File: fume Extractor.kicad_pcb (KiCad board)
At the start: 2 copper layers, 63.5 x 23.5 mm, 11 parts, among them J1 FAN, Q1 BC337, SW1 SW_SPST, U1 L7805ACV

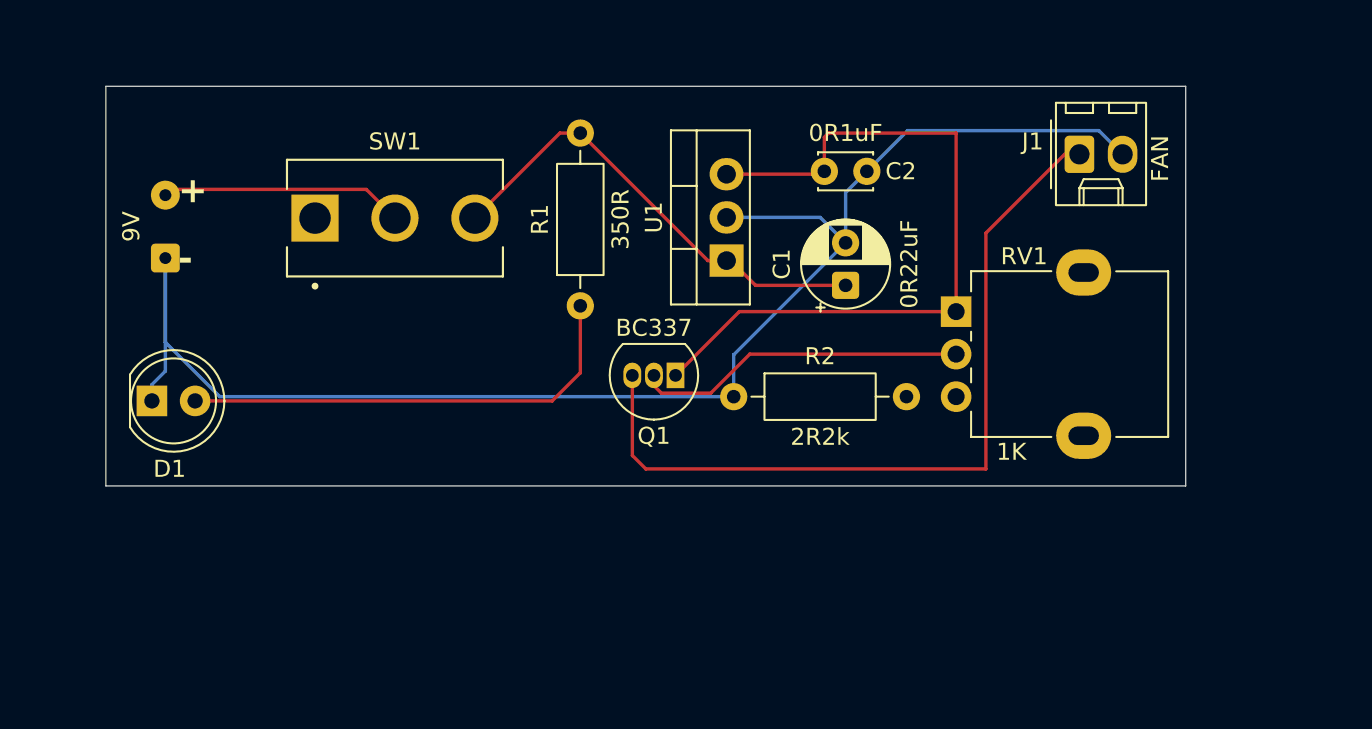
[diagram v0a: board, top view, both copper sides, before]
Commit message: fix: adjust pp cap and sizes
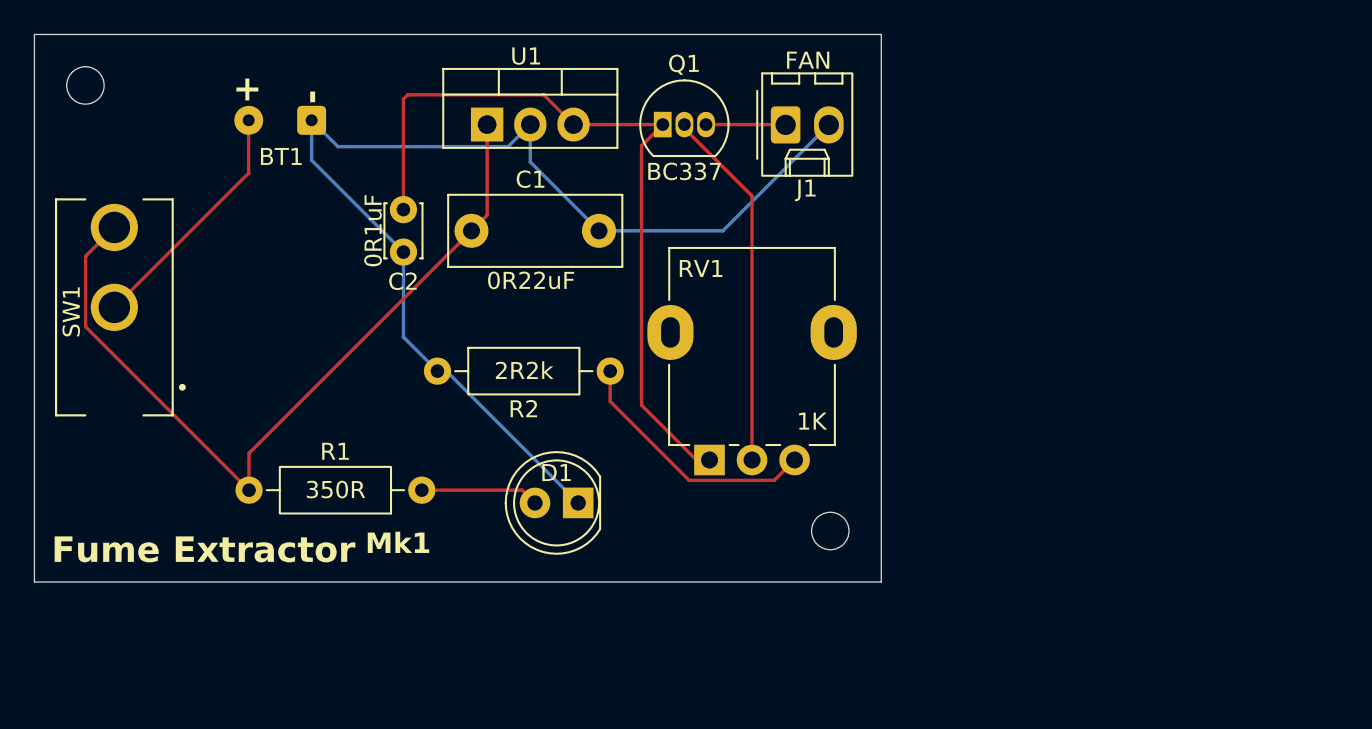
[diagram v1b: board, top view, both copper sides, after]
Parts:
- added ?: MountingHole_2.2mm_M2, MountingHole:MountingHole_2.2mm_M2, F.Cu at (69.8, 57.2)
- added REF**: MountingHole_2.2mm_M2, MountingHole:MountingHole_2.2mm_M2, F.Cu at (113.6, 83.4)
- C1: footprint Capacitor_THT:CP_Radial_D5.0mm_P2.50mm -> Capacitor_THT:C_Rect_L10.0mm_W4.0mm_P7.50mm_MKS4
- moved C2 27.7 mm to (88.5, 67.0), turned to 90 degrees
- moved D1 25.8 mm to (98.8, 81.8), turned to 180 degrees
- moved C1 22.2 mm to (92.5, 65.8), turned to 0 degrees
- moved R2 17.5 mm to (90.5, 74.0)
- moved J1 17.4 mm to (111.0, 59.5)
- moved SW1 17.3 mm to (71.5, 70.2), turned to 180 degrees
- moved RV1 16.9 mm to (106.5, 79.2), turned to 90 degrees
- moved U1 16.2 mm to (93.4, 59.5), turned to 0 degrees
- moved Q1 14.8 mm to (103.8, 59.5), turned to 0 degrees
- moved R1 14.3 mm to (89.6, 81.0), turned to 180 degrees
- moved BT1 6.59 mm to (79.4, 59.2), turned to 0 degrees
- renumbered 9V to BT1
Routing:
- net Net-(J1-VCC): track 47.1 -> 4.69 mm
- net -BATT: track 90.3 -> 67.4 mm
- net Net-(D1-Pad2): track 27.3 -> 6.97 mm
- net Net-(U1-IN): track 27.6 -> 47.4 mm
- net Net-(R2-Pad2): track 0.00 -> 15.0 mm
- net Net-(Q1-B): track 19.5 -> 21.4 mm
- net Net-(Q1-C): track 44.2 -> 44.9 mm
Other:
- board size 63.5 x 23.5 mm -> 49.8 x 32.2 mm
- board text added: "Fume Extractor^{ Mk1}"
- board text added: "WayWayWay"
- board text added: "^{Design:} Lucas Santos"

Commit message: feat: v2 with trimmer pot
Added RV2 to avoid long dead zones in RV1 because 500ohm is too much to
limit the 2V needed to minimally drive the fan, so the pot is largelly
dead. Adding a 1k 3266 Trimmer increases the ground resistance and the
floor voltage so we need to turn RV1 less to start the fan.

Plus, this gives a finer control over the fan speed itself
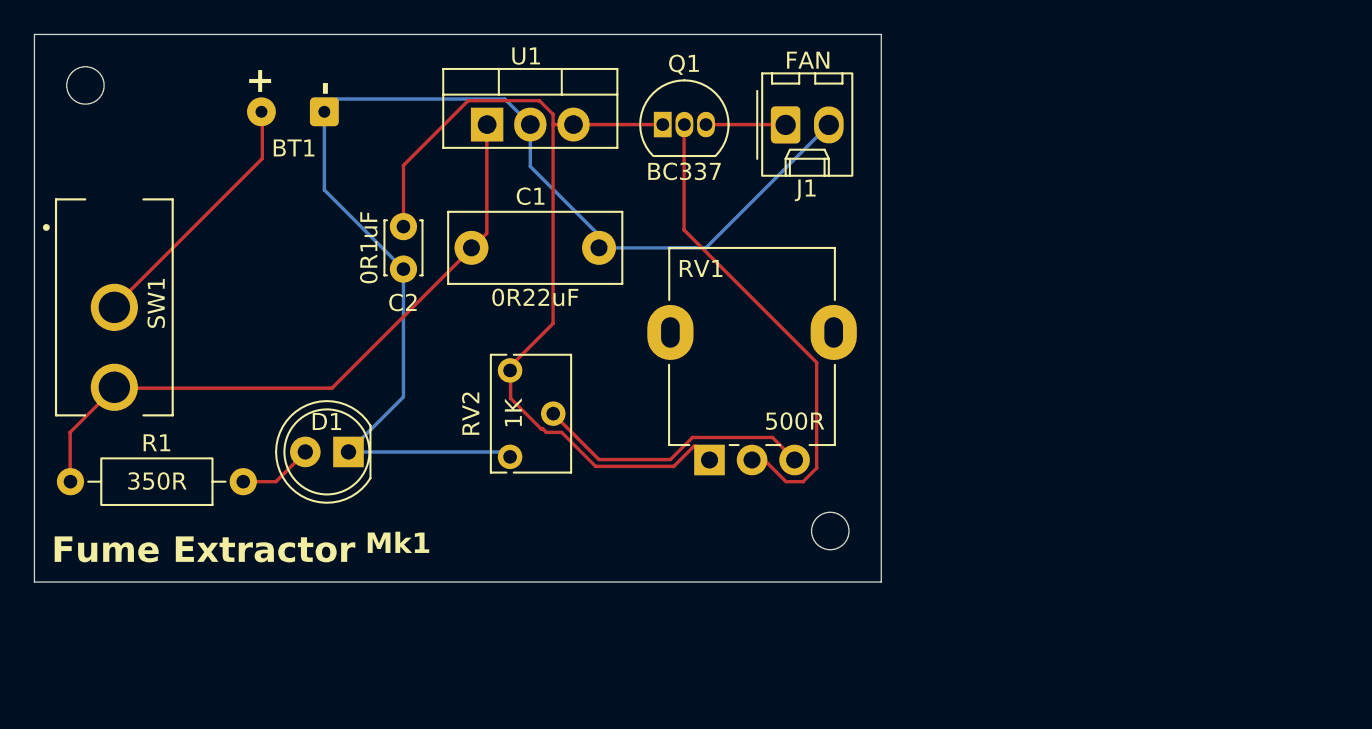
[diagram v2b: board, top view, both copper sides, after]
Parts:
- removed R2: 2R2k, Resistor_THT:R_Axial_DIN0207_L6.3mm_D2.5mm_P10.16mm_Horizontal
- added RV2: 1K, Potentiometer_THT:Potentiometer_Bourns_3266W_Vertical, F.Cu at (94.8, 74.0)
- RV1: value 1K -> 500R
- moved D1 13.8 mm to (85.3, 78.8)
- moved R1 10.5 mm to (79.1, 80.5)
- moved C1 1.00 mm to (92.5, 66.8)
- moved C2 1.00 mm to (88.5, 68.0)
- moved BT1 0.90 mm to (80.2, 58.8)
- turned SW1 to 0 degrees
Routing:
- net Net-(U1-IN): track 47.4 -> 38.6 mm
- net Net-(Q1-C): track 44.9 -> 52.4 mm
- net Net-(Q1-B): track 21.4 -> 28.1 mm
- net -BATT: track 67.4 -> 71.4 mm
- net Net-(D1-Pad2): track 6.97 -> 4.30 mm
- net Net-(RV1-Pad3): track 15.0 -> 16.4 mm
- net +9V: track 14.3 -> 15.0 mm

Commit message: Add Version 2
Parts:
- removed ?: MountingHole_2.2mm_M2, MountingHole:MountingHole_2.2mm_M2
- removed the REF** at (113.6, 83.4)
- added REF**: MountingHole_2.2mm_M2, MountingHole:MountingHole_2.2mm_M2, F.Cu at (104.4, 80.7)
- added REF**: MountingHole_2.2mm_M2, MountingHole:MountingHole_2.2mm_M2, F.Cu at (140.8, 90.3)
- BT1: footprint Connector_Wire:SolderWire-0.127sqmm_1x02_P3.7mm_D0.48mm_OD1mm -> Connector_Molex:Molex_KK-254_AE-6410-02A_1x02_P2.54mm_Vertical
- D1: value LED_5mm -> LED_3mm; footprint LED_THT:LED_D5.0mm -> LED_THT:LED_D3.0mm
- RV1: footprint Potentiometer_THT:Potentiometer_Alpha_RD901F-40-00D_Single_Vertical -> Connector_Wire:SolderWire-0.5sqmm_1x03_P4.6mm_D0.9mm_OD2.1mm
- SW1: footprint User_Passives:SW_SPDT_100SP1T1B4M2QE -> PCM_4ms_Switch:Switch_Toggle_SPDT_SubMini
- moved BT1 49.0 mm to (118.3, 89.4)
- moved C1 44.3 mm to (132.8, 85.2), turned to 180 degrees
- moved SW1 40.4 mm to (106.7, 90.0), turned to 90 degrees
- moved RV2 39.1 mm to (129.8, 91.4), turned to 180 degrees
- moved J1 39.1 mm to (139.8, 86.0), turned to 90 degrees
- moved Q1 37.5 mm to (124.4, 90.8)
- moved R1 36.3 mm to (115.0, 85.4)
- moved C2 35.3 mm to (121.8, 79.8), turned to -90 degrees
- moved D1 31.8 mm to (114.9, 90.2)
- moved U1 29.5 mm to (112.5, 82.0)
- moved RV1 18.6 mm to (125.1, 80.0), turned to 0 degrees
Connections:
- RV1 pad 1: Net-(Q1-C) -> Net-(RV1-Pad1)
- RV1 pad 3: Net-(RV1-Pad3) -> Net-(Q1-C)
- RV2 pad 2: Net-(RV1-Pad3) -> Net-(RV1-Pad1)
- SW1 pad 1: unconnected-(SW1-Pad1) -> Net-(U1-IN)
- SW1 pad 3: Net-(U1-IN) -> unconnected-(SW1-Pad3)
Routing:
- net Net-(Q1-C): track 52.4 -> 33.0 mm
- net -BATT: track 71.4 -> 52.9 mm, vias 0 -> 1
- net Net-(Q1-B): track 28.1 -> 11.6 mm
- net Net-(RV1-Pad3): track 16.4 -> 0.00 mm
- net Net-(J1-VCC): track 4.70 -> 16.3 mm, vias 0 -> 1
- net Net-(RV1-Pad1): track 0.00 -> 11.3 mm
- net Net-(U1-IN): track 38.6 -> 45.6 mm
- net Net-(D1-Pad2): track 4.30 -> 5.88 mm
- net +9V: track 15.0 -> 13.8 mm
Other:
- board size 49.8 x 32.2 mm -> 41.7 x 15 mm
- board text added: "+9V"
- board text added: "Fume Extractor^{ Mk2}"
- board text added: "GND"
- board text added: "ON"
- board text added: "VCC"
- board text removed: "Fume Extractor^{ Mk1}"
